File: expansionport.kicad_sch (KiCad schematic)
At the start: 18 parts, among them J20 C64_Expansion_Port, U22 74LS06N, U32 74LVC374, U33 74LVC374, U34 74LVC374, U35 74LS374, U36 74LS374, U37 74LS374, U38 74LVC374, U39 74LVC374, U40 74LS374, U41 74LS374, U42 74LS06

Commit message: more routing
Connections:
- net IRQ_N: now also U32.17 (D6); no longer U32.4 (D1)
- net ROMH_N: now also U32.4 (D1); no longer U32.17 (D6)
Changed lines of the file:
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@@
     (effects (font (size 1.27 1.27)) (justify right bottom))
   )
-  (label "ROMH_N" (at 101.6 154.94 180)
+  (label "ROMH_N" (at 101.6 142.24 180)
     (effects (font (size 1.27 1.27)) (justify right bottom))
   )
@@
     (effects (font (size 1.27 1.27)) (justify right bottom))
   )
-  (label "IRQ_N" (at 101.6 142.24 180)
+  (label "IRQ_N" (at 101.6 154.94 180)
     (effects (font (size 1.27 1.27)) (justify right bottom))
   )

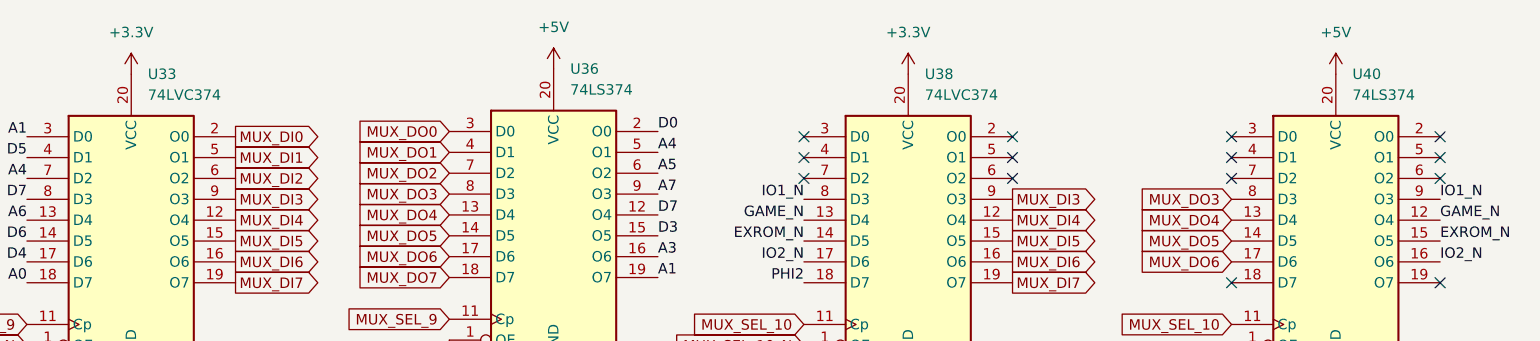
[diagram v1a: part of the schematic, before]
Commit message: add footprints to differentiate 3.3V from 5V ICs
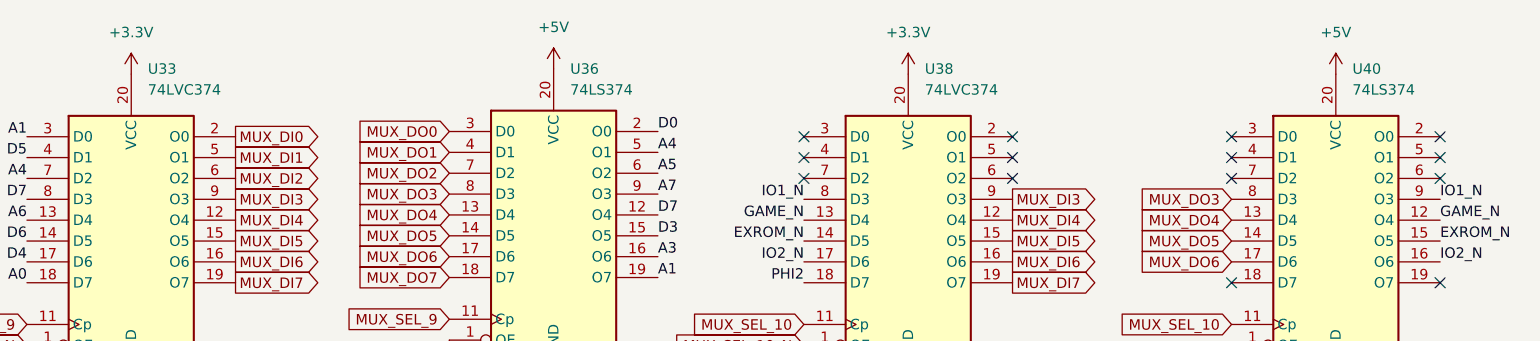
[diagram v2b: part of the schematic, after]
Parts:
- U32, U33, U34, U38, U39: footprint Package_DIP:DIP-20_W7.62mm -> snapeda:DIP-20_LVC_Family
- U35, U36, U37, U40, U41: footprint Package_DIP:DIP-20_W7.62mm -> snapeda:DIP-20_LS_Family
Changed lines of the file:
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@@
       (effects (font (size 1.27 1.27)) (justify left))
     )
-    (property "Footprint" "Package_DIP:DIP-20_W7.62mm" (id 2) (at 262.89 96.52 0)
+    (property "Footprint" "snapeda:DIP-20_LS_Family" (id 2) (at 262.89 96.52 0)
       (effects (font (size 1.27 1.27)) hide)
     )
@@
       (effects (font (size 1.27 1.27)) (justify left))
     )
-    (property "Footprint" "Package_DIP:DIP-20_W7.62mm" (id 2) (at 116.205 96.52 0)
+    (property "Footprint" "snapeda:DIP-20_LVC_Family" (id 2) (at 116.205 96.52 0)
       (effects (font (size 1.27 1.27)) hide)
     )
@@
       (effects (font (size 1.27 1.27)) (justify left))
     )
-    (property "Footprint" "Package_DIP:DIP-20_W7.62mm" (id 2) (at 114.3 152.4 0)
+    (property "Footprint" "snapeda:DIP-20_LVC_Family" (id 2) (at 114.3 152.4 0)
       (effects (font (size 1.27 1.27)) hide)
     )
@@
   (symbol (lib_id "74xx:74HC374") (at 116.205 41.275 0) (unit 1)
     (in_bom yes) (on_board yes) (fields_autoplaced)
-    (property "Reference" "U33" (id 0) (at 118.2244 20.955 0)
-      (effects (font (size 1.27 1.27)) (justify left))
-    )
-    (property "Value" "74LVC374" (id 1) (at 118.2244 23.495 0)
-      (effects (font (size 1.27 1.27)) (justify left))
-    )
-    (property "Footprint" "Package_DIP:DIP-20_W7.62mm" (id 2) (at 116.205 41.275 0)
+    (property "Reference" "U33" (id 0) (at 118.2244 20.32 0)
+      (effects (font (size 1.27 1.27)) (justify left))
+    )
+    (property "Value" "74LVC374" (id 1) (at 118.2244 22.86 0)
+      (effects (font (size 1.27 1.27)) (justify left))
+    )
+    (property "Footprint" "snapeda:DIP-20_LVC_Family" (id 2) (at 116.205 41.275 0)
       (effects (font (size 1.27 1.27)) hide)
     )
@@
   (symbol (lib_id "74xx:74LS374") (at 262.89 41.275 0) (unit 1)
     (in_bom yes) (on_board yes) (fields_autoplaced)
-    (property "Reference" "U40" (id 0) (at 264.9094 20.955 0)
-      (effects (font (size 1.27 1.27)) (justify left))
-    )
-    (property "Value" "74LS374" (id 1) (at 264.9094 23.495 0)
-      (effects (font (size 1.27 1.27)) (justify left))
-    )
-    (property "Footprint" "Package_DIP:DIP-20_W7.62mm" (id 2) (at 262.89 41.275 0)
+    (property "Reference" "U40" (id 0) (at 264.9094 20.32 0)
+      (effects (font (size 1.27 1.27)) (justify left))
+    )
+    (property "Value" "74LS374" (id 1) (at 264.9094 22.86 0)
+      (effects (font (size 1.27 1.27)) (justify left))
+    )
+    (property "Footprint" "snapeda:DIP-20_LS_Family" (id 2) (at 262.89 41.275 0)
       (effects (font (size 1.27 1.27)) hide)
     )
@@
       (effects (font (size 1.27 1.27)) (justify left))
     )
-    (property "Footprint" "Package_DIP:DIP-20_W7.62mm" (id 2) (at 167.64 40.64 0)
+    (property "Footprint" "snapeda:DIP-20_LS_Family" (id 2) (at 167.64 40.64 0)
       (effects (font (size 1.27 1.27)) hide)
     )
@@
       (effects (font (size 1.27 1.27)) (justify left))
     )
-    (property "Footprint" "Package_DIP:DIP-20_W7.62mm" (id 2) (at 210.82 96.52 0)
+    (property "Footprint" "snapeda:DIP-20_LVC_Family" (id 2) (at 210.82 96.52 0)
       (effects (font (size 1.27 1.27)) hide)
     )
@@
       (effects (font (size 1.27 1.27)) (justify left))
     )
-    (property "Footprint" "Package_DIP:DIP-20_W7.62mm" (id 2) (at 166.37 152.4 0)
+    (property "Footprint" "snapeda:DIP-20_LS_Family" (id 2) (at 166.37 152.4 0)
       (effects (font (size 1.27 1.27)) hide)
     )
@@
       (effects (font (size 1.27 1.27)) (justify left))
     )
-    (property "Footprint" "Package_DIP:DIP-20_W7.62mm" (id 2) (at 167.64 96.52 0)
+    (property "Footprint" "snapeda:DIP-20_LS_Family" (id 2) (at 167.64 96.52 0)
       (effects (font (size 1.27 1.27)) hide)
     )
@@
   (symbol (lib_id "74xx:74HC374") (at 210.82 41.275 0) (unit 1)
     (in_bom yes) (on_board yes) (fields_autoplaced)
-    (property "Reference" "U38" (id 0) (at 212.8394 20.955 0)
-      (effects (font (size 1.27 1.27)) (justify left))
-    )
-    (property "Value" "74LVC374" (id 1) (at 212.8394 23.495 0)
-      (effects (font (size 1.27 1.27)) (justify left))
-    )
-    (property "Footprint" "Package_DIP:DIP-20_W7.62mm" (id 2) (at 210.82 41.275 0)
-      (effects (font (size 1.27 1.27)) hide)
-    )
+    (property "Reference" "U38" (id 0) (at 212.8394 20.32 0)
+      (effects (font (size 1.27 1.27)) (justify left))
+    )
+    (property "Value" "74LVC374" (id 1) (at 212.8394 22.86 0)
+      (effects (font (size 1.27 1.27)) (justify left))
+    )
+    (property "Footprint" "snapeda:DIP-20_LVC_Family" (id 2) (at 210.82 41.275 0)
+      (effects (font (size 1.27 1.27)) hide)
+    )

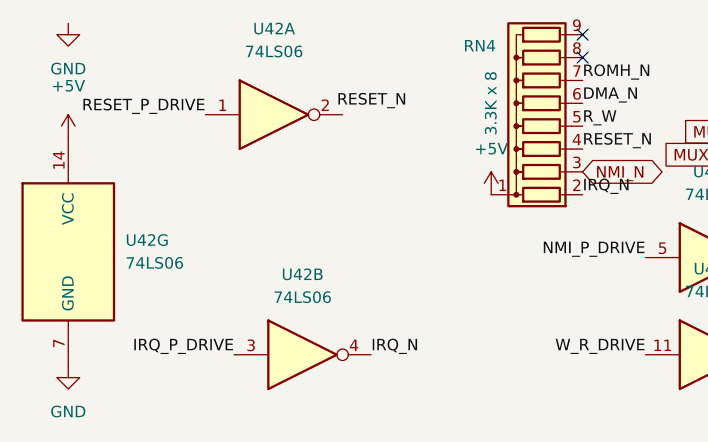
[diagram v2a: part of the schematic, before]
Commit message: re-do many labels and DRC fixes
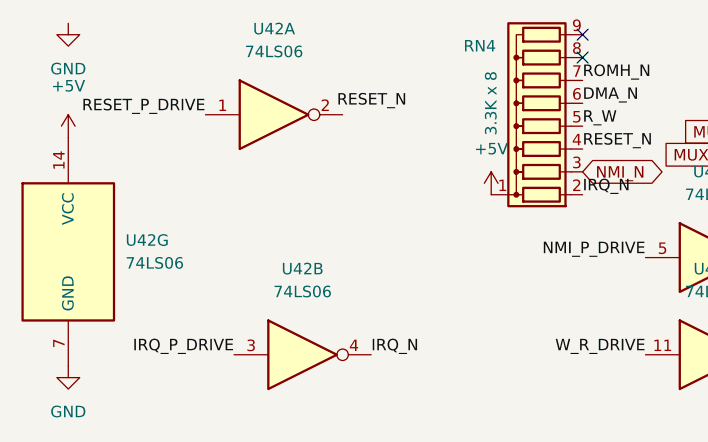
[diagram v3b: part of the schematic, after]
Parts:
- U22, U42: footprint Package_DIP:DIP-14_W7.62mm -> snapeda:DIP-14_74LS06
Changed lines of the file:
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@@
       (effects (font (size 1.27 1.27)) (justify left))
     )
-    (property "Footprint" "Package_DIP:DIP-14_W7.62mm" (id 2) (at 19.685 175.895 0)
+    (property "Footprint" "snapeda:DIP-14_74LS06" (id 2) (at 19.685 175.895 0)
       (effects (font (size 1.27 1.27)) hide)
     )
@@
   (symbol (lib_id "74xx:74LS06") (at 45.72 187.325 0) (unit 2)
     (in_bom yes) (on_board yes) (fields_autoplaced)
-    (property "Reference" "U42" (id 0) (at 45.72 178.435 0))
-    (property "Value" "74LS06" (id 1) (at 45.72 180.975 0))
-    (property "Footprint" "Package_DIP:DIP-14_W7.62mm" (id 2) (at 45.72 187.325 0)
+    (property "Reference" "U42" (id 0) (at 45.72 177.8 0))
+    (property "Value" "74LS06" (id 1) (at 45.72 180.34 0))
+    (property "Footprint" "snapeda:DIP-14_74LS06" (id 2) (at 45.72 187.325 0)
       (effects (font (size 1.27 1.27)) hide)
     )
@@
     (property "Reference" "U42" (id 0) (at 91.44 167.005 0))
     (property "Value" "74LS06" (id 1) (at 91.44 169.545 0))
-    (property "Footprint" "Package_DIP:DIP-14_W7.62mm" (id 2) (at 91.44 176.53 0)
+    (property "Footprint" "snapeda:DIP-14_74LS06" (id 2) (at 91.44 176.53 0)
       (effects (font (size 1.27 1.27)) hide)
     )
@@
     (property "Reference" "U42" (id 0) (at 139.065 167.64 0))
     (property "Value" "74LS06" (id 1) (at 139.065 170.18 0))
-    (property "Footprint" "Package_DIP:DIP-14_W7.62mm" (id 2) (at 139.065 176.53 0)
+    (property "Footprint" "snapeda:DIP-14_74LS06" (id 2) (at 139.065 176.53 0)
       (effects (font (size 1.27 1.27)) hide)
     )
@@
     (property "Reference" "U42" (id 0) (at 42.545 151.13 0))
     (property "Value" "74LS06" (id 1) (at 42.545 153.67 0))
-    (property "Footprint" "Package_DIP:DIP-14_W7.62mm" (id 2) (at 42.545 160.655 0)
+    (property "Footprint" "snapeda:DIP-14_74LS06" (id 2) (at 42.545 160.655 0)
       (effects (font (size 1.27 1.27)) hide)
     )
@@
     (property "Reference" "U42" (id 0) (at 139.065 178.435 0))
     (property "Value" "74LS06" (id 1) (at 139.065 180.975 0))
-    (property "Footprint" "Package_DIP:DIP-14_W7.62mm" (id 2) (at 139.065 187.325 0)
+    (property "Footprint" "snapeda:DIP-14_74LS06" (id 2) (at 139.065 187.325 0)
       (effects (font (size 1.27 1.27)) hide)
     )
@@
     (property "Reference" "U42" (id 0) (at 91.44 177.8 0))
     (property "Value" "74LS06" (id 1) (at 91.44 180.34 0))
-    (property "Footprint" "Package_DIP:DIP-14_W7.62mm" (id 2) (at 91.44 187.325 0)
+    (property "Footprint" "snapeda:DIP-14_74LS06" (id 2) (at 91.44 187.325 0)
       (effects (font (size 1.27 1.27)) hide)
     )
@@
     (property "Reference" "U22" (id 0) (at 44.45 106.68 0))
     (property "Value" "74LS06N" (id 1) (at 44.45 109.22 0))
-    (property "Footprint" "Package_DIP:DIP-14_W7.62mm" (id 2) (at 44.45 116.205 0)
-      (effects (font (size 1.27 1.27)) hide)
-    )
+    (property "Footprint" "snapeda:DIP-14_74LS06" (id 2) (at 44.45 116.205 0)
+      (effects (font (size 1.27 1.27)) hide)
+    )

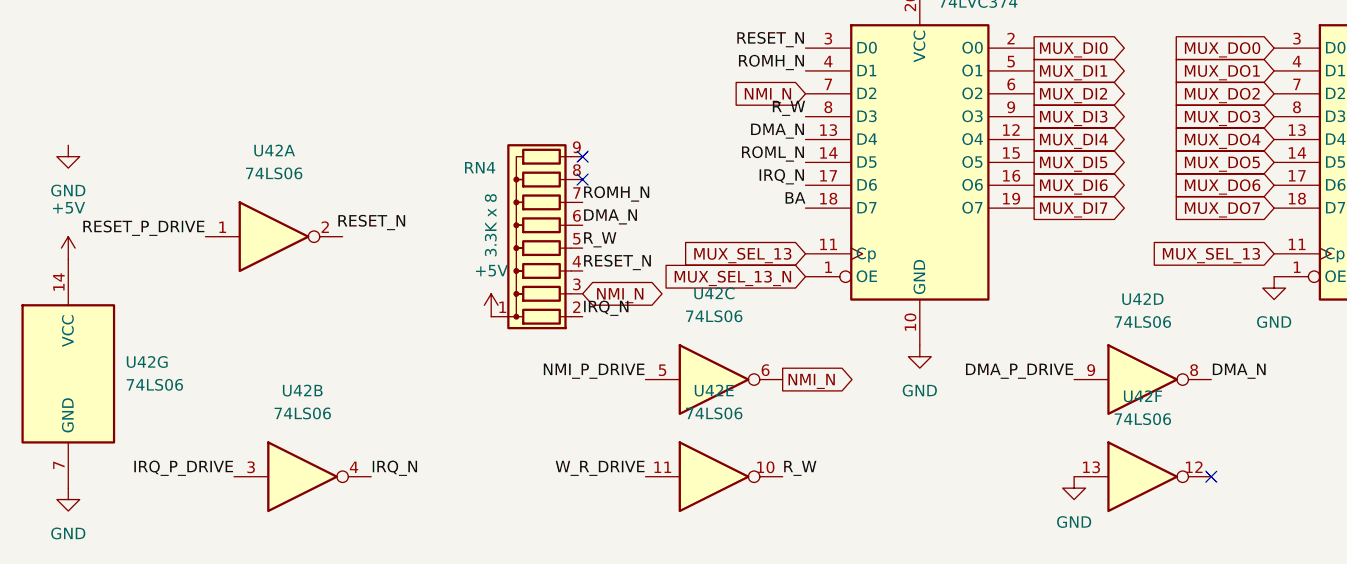
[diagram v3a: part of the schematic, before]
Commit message: work on BOM generation
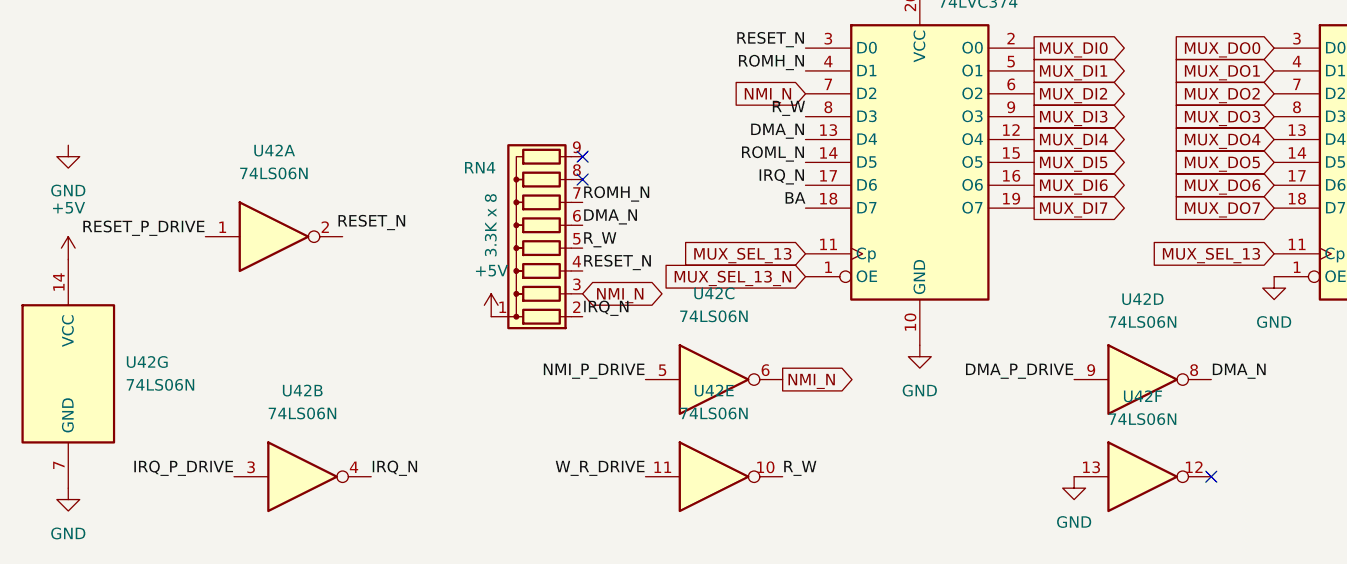
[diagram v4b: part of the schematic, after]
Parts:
- U42: value 74LS06 -> 74LS06N
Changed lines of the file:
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@@
       (effects (font (size 1.27 1.27)) (justify left))
     )
-    (property "Value" "74LS06" (id 1) (at 26.035 177.1649 0)
+    (property "Value" "74LS06N" (id 1) (at 26.035 177.1649 0)
       (effects (font (size 1.27 1.27)) (justify left))
     )
@@
     (in_bom yes) (on_board yes) (fields_autoplaced)
     (property "Reference" "U42" (id 0) (at 45.72 177.8 0))
-    (property "Value" "74LS06" (id 1) (at 45.72 180.34 0))
+    (property "Value" "74LS06N" (id 1) (at 45.72 180.34 0))
     (property "Footprint" "snapeda:DIP-14_74LS06" (id 2) (at 45.72 187.325 0)
       (effects (font (size 1.27 1.27)) hide)
@@
     (in_bom yes) (on_board yes) (fields_autoplaced)
     (property "Reference" "U42" (id 0) (at 91.44 167.005 0))
-    (property "Value" "74LS06" (id 1) (at 91.44 169.545 0))
+    (property "Value" "74LS06N" (id 1) (at 91.44 169.545 0))
     (property "Footprint" "snapeda:DIP-14_74LS06" (id 2) (at 91.44 176.53 0)
       (effects (font (size 1.27 1.27)) hide)
@@
     (in_bom yes) (on_board yes) (fields_autoplaced)
     (property "Reference" "U42" (id 0) (at 139.065 167.64 0))
-    (property "Value" "74LS06" (id 1) (at 139.065 170.18 0))
+    (property "Value" "74LS06N" (id 1) (at 139.065 170.18 0))
     (property "Footprint" "snapeda:DIP-14_74LS06" (id 2) (at 139.065 176.53 0)
       (effects (font (size 1.27 1.27)) hide)
@@
     (in_bom yes) (on_board yes) (fields_autoplaced)
     (property "Reference" "U42" (id 0) (at 42.545 151.13 0))
-    (property "Value" "74LS06" (id 1) (at 42.545 153.67 0))
+    (property "Value" "74LS06N" (id 1) (at 42.545 153.67 0))
     (property "Footprint" "snapeda:DIP-14_74LS06" (id 2) (at 42.545 160.655 0)
       (effects (font (size 1.27 1.27)) hide)
@@
     (in_bom yes) (on_board yes) (fields_autoplaced)
     (property "Reference" "U42" (id 0) (at 139.065 178.435 0))
-    (property "Value" "74LS06" (id 1) (at 139.065 180.975 0))
+    (property "Value" "74LS06N" (id 1) (at 139.065 180.975 0))
     (property "Footprint" "snapeda:DIP-14_74LS06" (id 2) (at 139.065 187.325 0)
       (effects (font (size 1.27 1.27)) hide)
@@
     (in_bom yes) (on_board yes) (fields_autoplaced)
     (property "Reference" "U42" (id 0) (at 91.44 177.8 0))
-    (property "Value" "74LS06" (id 1) (at 91.44 180.34 0))
+    (property "Value" "74LS06N" (id 1) (at 91.44 180.34 0))
     (property "Footprint" "snapeda:DIP-14_74LS06" (id 2) (at 91.44 187.325 0)
       (effects (font (size 1.27 1.27)) hide)
